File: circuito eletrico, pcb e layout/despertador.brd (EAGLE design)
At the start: 95 x 55 mm, 9 parts, among them IC1 MEGA8-P

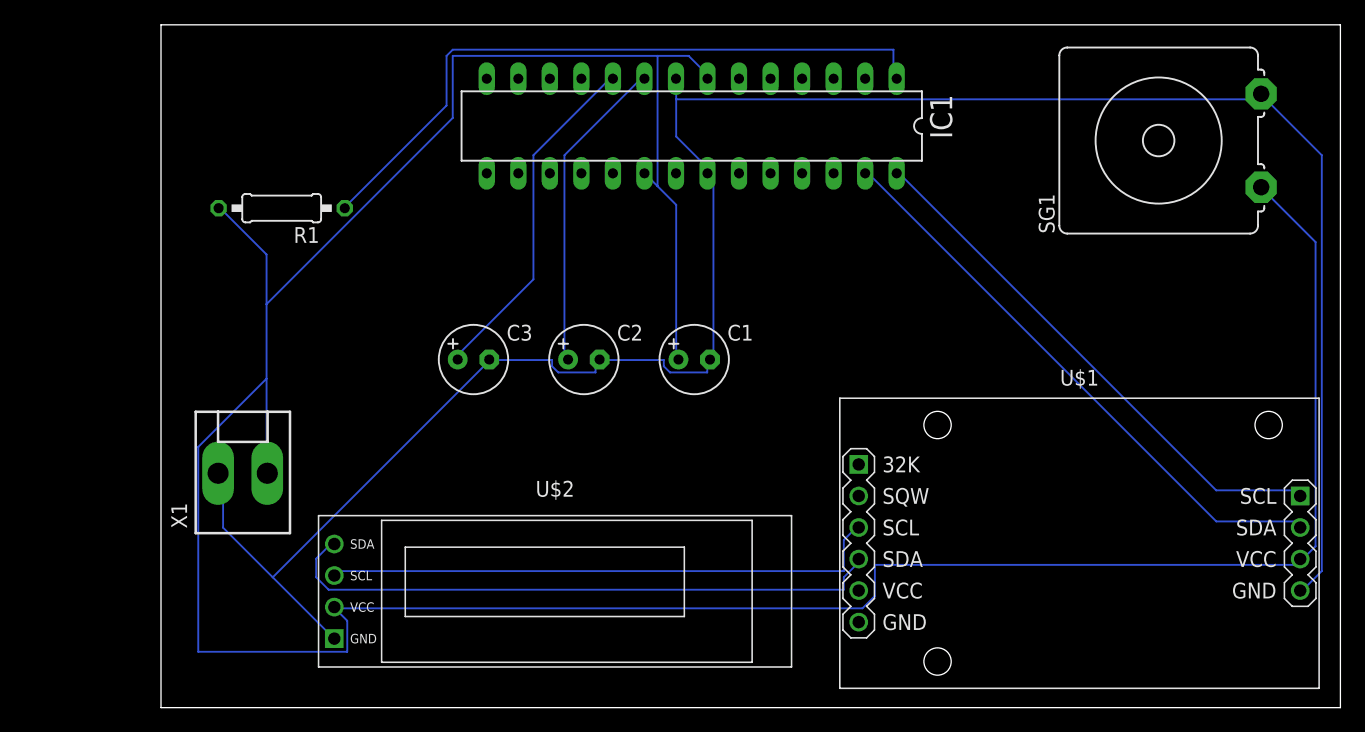
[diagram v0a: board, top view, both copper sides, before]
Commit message: Adicionado USB nos componentes
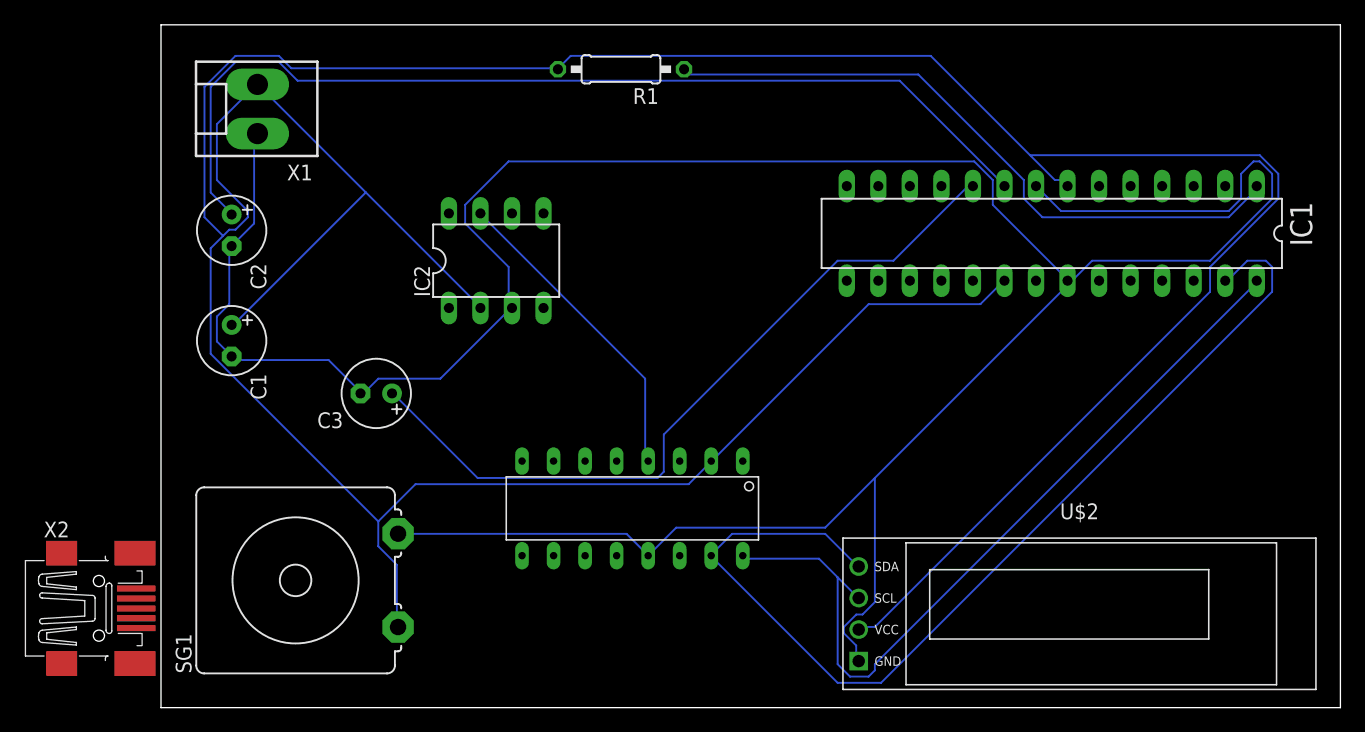
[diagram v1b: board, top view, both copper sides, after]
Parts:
- removed U$1: RTC-DS3231-AT24C32, diy-modules:RTC-DS3231-AT24C32
- added IC2: MAX702CPA, maxim:DIL08
- added U$3: DS3231, Microcontroladores:PDIP
- added X2: MINI-USB-32005-201, con-cypressindustries:32005-201
- moved SG1 78.0 mm to (10.8, 10.2)
- moved U$2 42.3 mm to (74.0, 7.56)
- moved C1 37.3 mm to (5.69, 29.6), turned to 270 degrees
- moved IC1 30.3 mm to (71.8, 38.2)
- moved C2 30.2 mm to (5.69, 38.5), turned to 270 degrees
- moved R1 29.5 mm to (37.0, 51.4)
- moved X1 29.4 mm to (7.77, 48.2), turned to 90 degrees
- moved C3 8.29 mm to (17.3, 25.3), turned to 180 degrees
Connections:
- removed net GND.1: U$1.J1.6
- removed net N$7: U$1.J1.3, U$2.3
- removed net VCC.1: U$1.J1.5
- net GND: now also IC2.3, U$3.13; no longer U$1.J2.4
- net N$1: now also U$2.4, U$3.15; no longer U$1.J2.2
- net N$5: now also U$2.3, U$3.16; no longer U$1.J2.1
- net N$6: now also IC2.7, U$3.4; no longer U$1.J1.4, U$2.4
- net VCC: now also IC2.2, U$3.2; no longer U$1.J2.3
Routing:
- net VCC: track 250.9 -> 313.7 mm
- net GND: track 177.9 -> 236.4 mm
- net N$2: track 25.5 -> 79.9 mm
- net N$7: track 45.5 -> 0.00 mm
- net N$1: track 46.9 -> 82.8 mm
- net N$3: track 27.9 -> 61.1 mm
- net N$6: track 49.2 -> 25.6 mm
- net N$5: track 43.3 -> 65.5 mm
- net N$4: track 54.3 -> 53.5 mm
